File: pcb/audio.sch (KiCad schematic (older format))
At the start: 32 parts, among them J1 AudioJack3_SwitchTR, U400 CS43130, U401 ADP150-3.0, U402 ADP150-1.8, U403 ADP150-1.8, X1 DSC1001CE2-022.5792

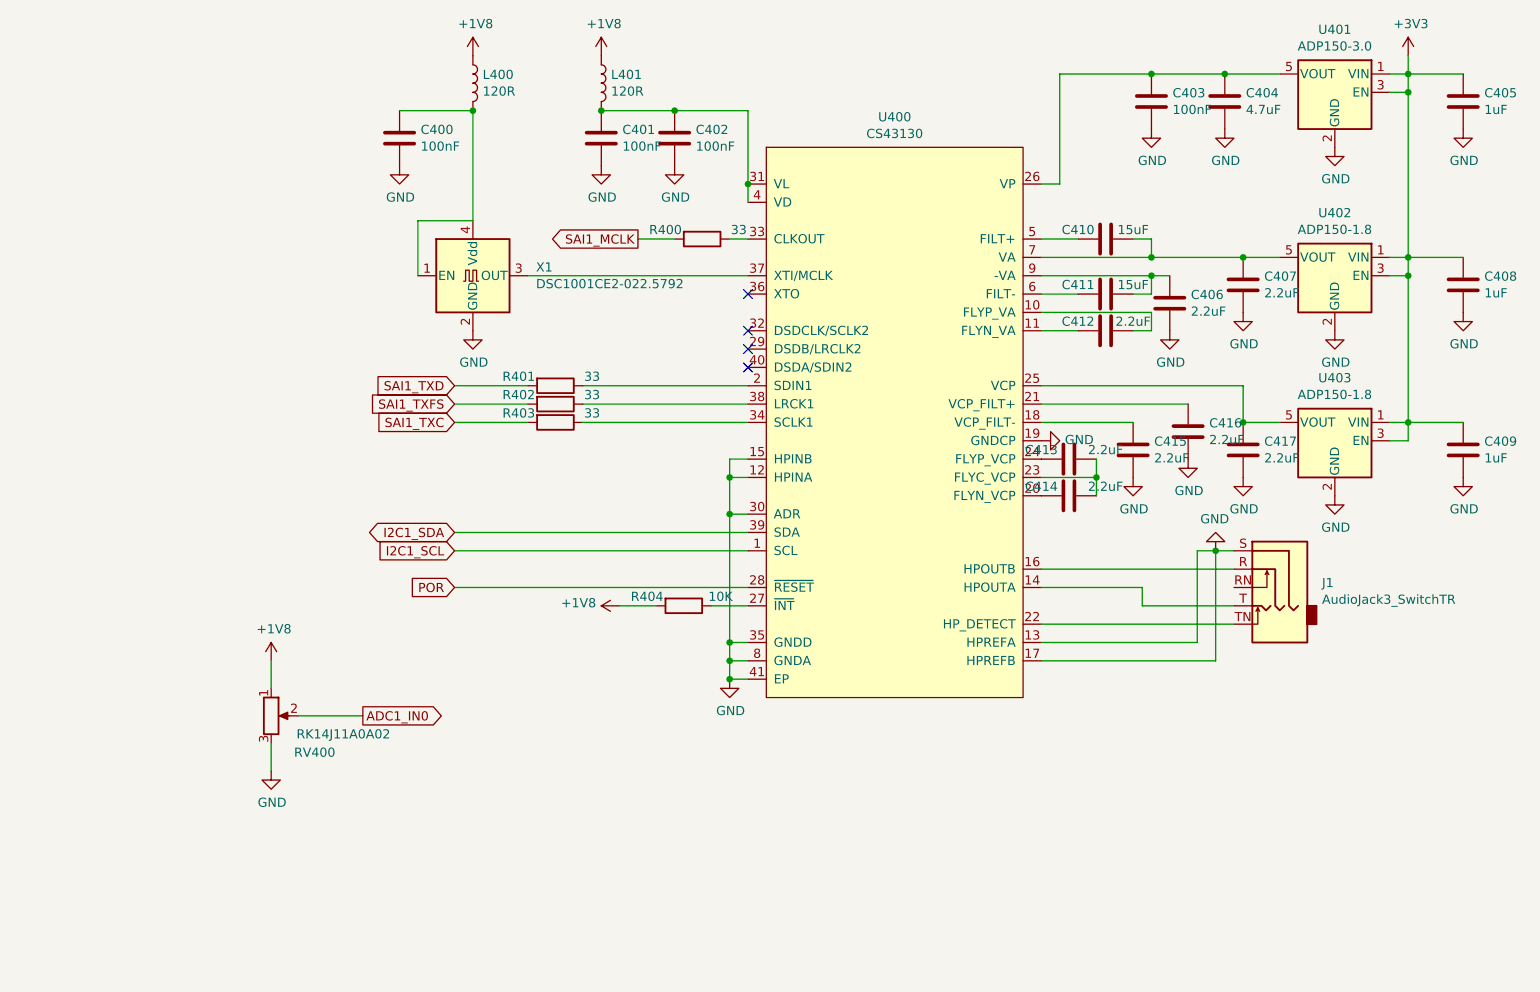
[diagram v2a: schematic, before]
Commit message: pcb: fixing voltage domain
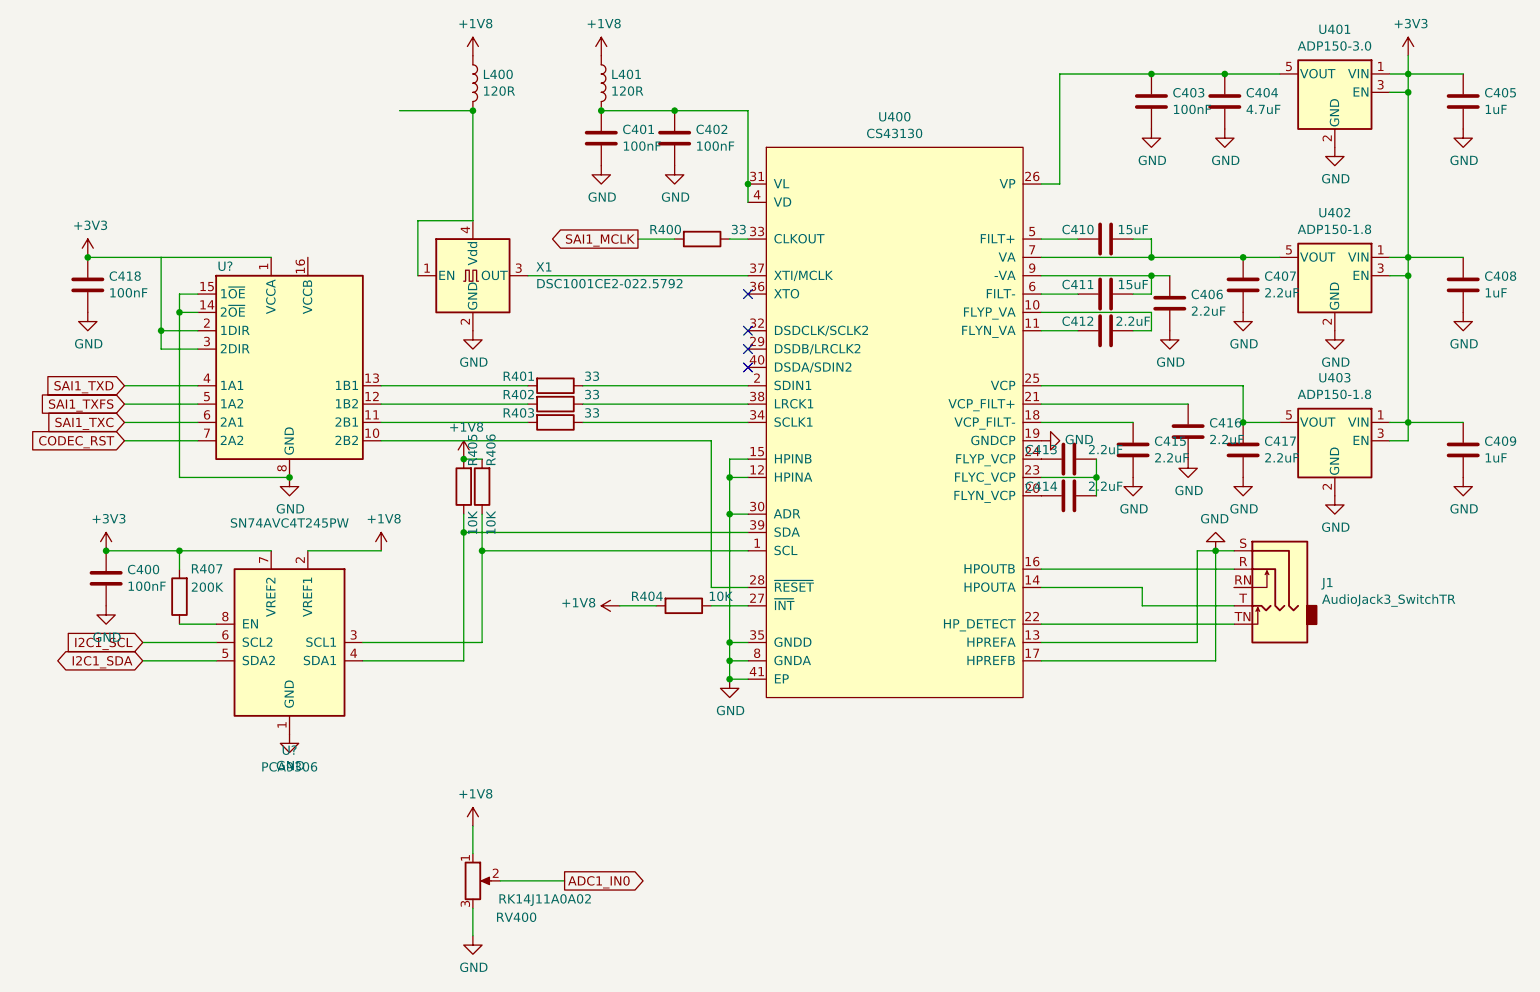
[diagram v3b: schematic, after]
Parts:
- added C418: 100nF, Capacitor_SMD:C_0402_1005Metric, symbol Device:C
- added R405, R406: 10K, Resistor_SMD:R_0603_1608Metric, symbol Device:R
- added R407: 200K, Resistor_SMD:R_0603_1608Metric, symbol Device:R
- added U?: SN74AVC4T245PW, Package_SO:TSSOP-16_4.4x5mm_P0.65mm, symbol Logic_LevelTranslator:SN74AVC4T245PW
- added U?: PCA9306, symbol Interface:PCA9306
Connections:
- net +1V8: now also R405.2, R406.2, U?.2 (VREF1)
- net +3V3: now also C400.1, C418.1, R407.2, U?.1 (VCCA), U?.2 (1DIR), U?.3 (2DIR), U?.7 (VREF2)
- net GND: now also C418.2, U?.1 (GND), U?.14 (2~OE), U?.15 (1~OE), U?.8 (GND), U?.9 (GND)
- net I2C1_SCL: now also U?.6 (SCL2); no longer U400.1 (SCL)
- net I2C1_SDA: now also U?.5 (SDA2); no longer U400.39 (SDA)
- net SAI1_TXC: now also U?.6 (2A1); no longer R403.2
- net SAI1_TXD: now also U?.4 (1A1); no longer R401.2
- net SAI1_TXFS: now also U?.5 (1A2); no longer R402.2
- net at L400.2, X1.1 (EN), X1.4 (Vdd): no longer C400.1
- net POR: no longer names the net of U400.28 (~RESET)
- net POR: now also U?.10 (2B2)
- new net: R406.1, U400.1 (SCL), U?.3 (SCL1)
- new net: R405.1, U400.39 (SDA), U?.4 (SDA1)
- new net: R401.2, U?.13 (1B1)
- new net: R402.2, U?.12 (1B2)
- new net: R403.2, U?.11 (2B1)
- new net: R407.1, U?.8 (EN)
- new net CODEC_RST: U?.7 (2A2)
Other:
- moved on the sheet: C400, RV400

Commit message: pcb: fixing i2c numbering; add filtering for lcd
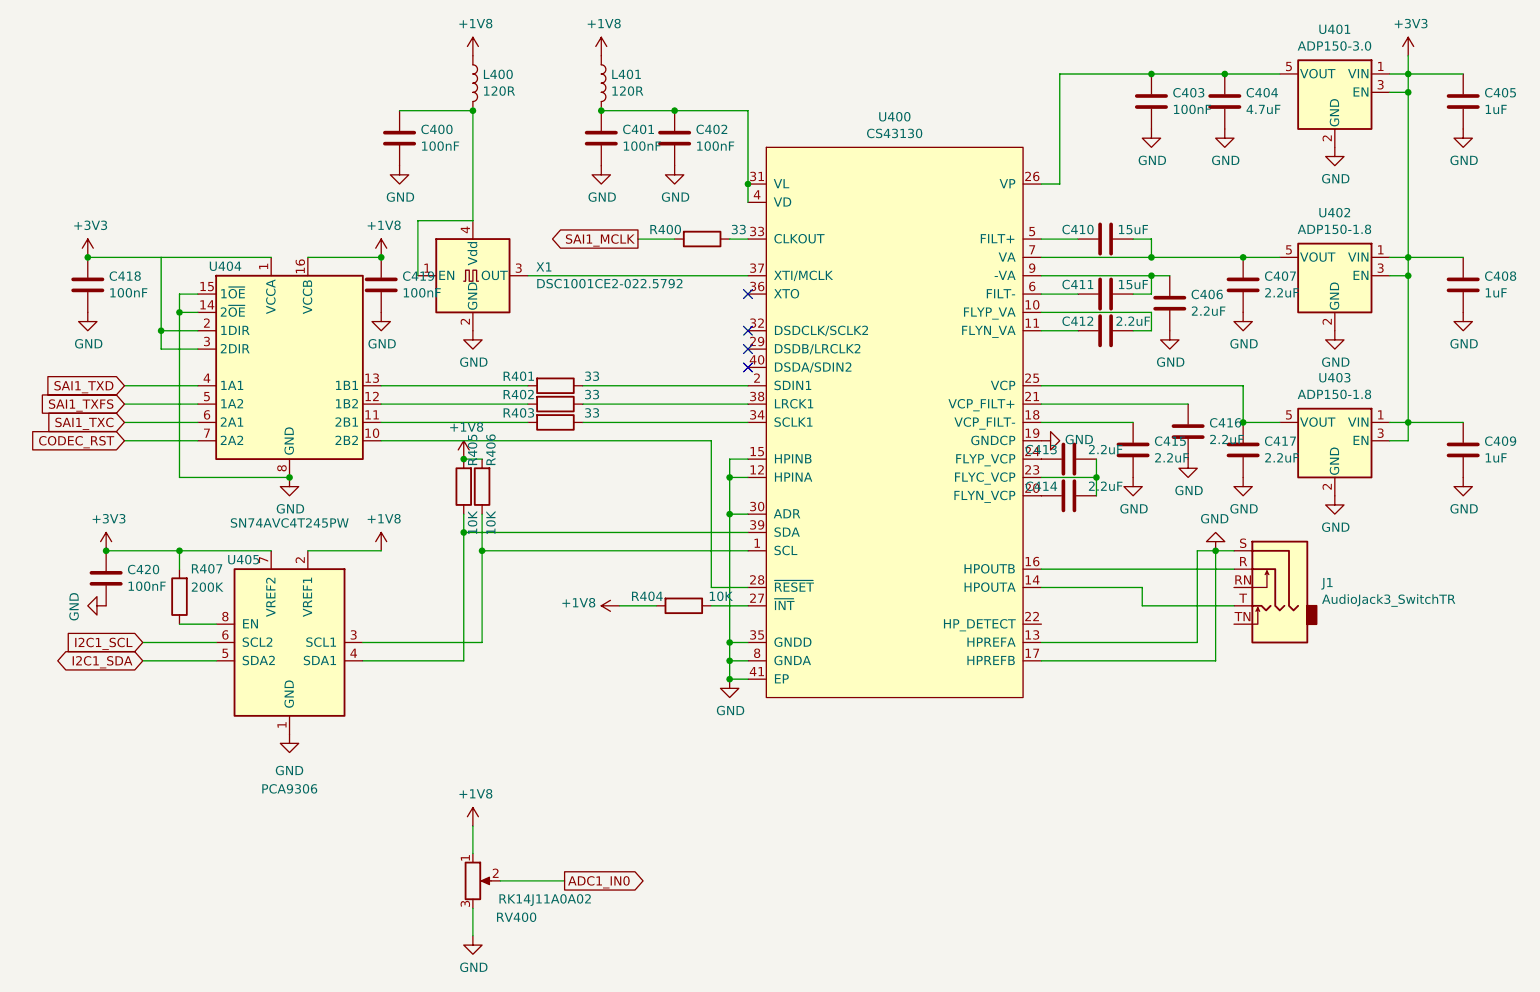
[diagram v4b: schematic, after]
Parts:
- added C419, C420: 100nF, Capacitor_SMD:C_0402_1005Metric, symbol Device:C
- U405: renamed from U?; footprint (none) -> Package_SO:VSSOP-8_2.3x2mm_P0.5mm
- gave numbers to parts that had none: 1
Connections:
- net +1V8: now also U404.16 (VCCB), C419.1
- net +3V3: now also C420.1; no longer C400.1
- net GND: now also C419.2, C420.2
- net at U400.22 (HP_DETECT): no longer J1.TN
- net at L400.2, X1.1 (EN), X1.4 (Vdd): now also C400.1
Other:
- moved on the sheet: C400
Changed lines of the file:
@@
 L Device:C C400
 U 1 1 5D487832
-P 1500 5150
-F 0 "C400" H 1615 5196 50  0000 L CNN
-F 1 "100nF" H 1615 5105 50  0000 L CNN
-F 2 "Capacitor_SMD:C_0402_1005Metric" H 1538 5000 50  0001 C CNN
-F 3 "~" H 1500 5150 50  0001 C CNN
-	1    1500 5150
+P 3100 2750
+F 0 "C400" H 3215 2796 50  0000 L CNN
+F 1 "100nF" H 3215 2705 50  0000 L CNN
+F 2 "Capacitor_SMD:C_0402_1005Metric" H 3138 2600 50  0001 C CNN
+F 3 "~" H 3100 2750 50  0001 C CNN
+	1    3100 2750
 	1    0    0    -1
 $EndComp
@@
 L power:GND #PWR0273
 U 1 1 5D487838
-P 1500 5300
-F 0 "#PWR0273" H 1500 5050 50  0001 C CNN
-F 1 "GND" H 1505 5127 50  0000 C CNN
-F 2 "" H 1500 5300 50  0001 C CNN
-F 3 "" H 1500 5300 50  0001 C CNN
-	1    1500 5300
+P 3100 2900
+F 0 "#PWR0273" H 3100 2650 50  0001 C CNN
+F 1 "GND" H 3105 2727 50  0000 C CNN
+F 2 "" H 3100 2900 50  0001 C CNN
+F 3 "" H 3100 2900 50  0001 C CNN
+	1    3100 2900
 	1    0    0    -1
 $EndComp
@@
 $EndComp
 Wire Wire Line
-	6600 5400 7650 5400
-Wire Wire Line
 	5000 4500 4900 4500
 Wire Wire Line
@@
 $EndComp
 $Comp
-L Logic_LevelTranslator:SN74AVC4T245PW U?
+L Logic_LevelTranslator:SN74AVC4T245PW U404
 U 1 1 5D8C4C20
 P 2500 4000
-F 0 "U?" H 2150 4550 50  0000 C CNN
+F 0 "U404" H 2150 4550 50  0000 C CNN
 F 1 "SN74AVC4T245PW" H 2500 3150 50  0000 C CNN
 F 2 "Package_SO:TSSOP-16_4.4x5mm_P0.65mm" H 2500 3900 50  0001 C CNN
@@
 	3450 4900 5000 4900
 $Comp
-L Interface:PCA9306 U?
+L Interface:PCA9306 U405
 U 1 1 5D90AA81
 P 2500 5500
-F 0 "U?" H 2500 4911 50  0000 C CNN
-F 1 "PCA9306" H 2500 4820 50  0000 C CNN
-F 2 "" H 2100 5850 50  0001 C CNN
+F 0 "U405" H 2750 5950 50  0000 C CNN
+F 1 "PCA9306" H 2500 4700 50  0000 C CNN
+F 2 "Package_SO:VSSOP-8_2.3x2mm_P0.5mm" H 2100 5850 50  0001 C CNN
 F 3 "http://www.ti.com/lit/ds/symlink/pca9306.pdf" H 2200 5950 50  0001 C CNN
 	1    2500 5500
@@
 Connection ~ 3550 5000
 $Comp
-L power:+1V8 #PWR?
+L power:+1V8 #PWR0120
 U 1 1 5D939A35
 P 3450 4500
-F 0 "#PWR?" H 3450 4350 50  0001 C CNN
+F 0 "#PWR0120" H 3450 4350 50  0001 C CNN
 F 1 "+1V8" H 3465 4673 50  0000 C CNN
 F 2 "" H 3450 4500 50  0001 C CNN
@@
 	1600 4400 2000 4400
 $Comp
-L power:GND #PWR?
+L power:GND #PWR0121
 U 1 1 5D94B448
 P 2500 4600
-F 0 "#PWR?" H 2500 4350 50  0001 C CNN
+F 0 "#PWR0121" H 2500 4350 50  0001 C CNN
 F 1 "GND" H 2505 4427 50  0000 C CNN
 F 2 "" H 2500 4600 50  0001 C CNN
@@
 $EndComp
 $Comp
-L power:GND #PWR?
+L power:GND #PWR0122
 U 1 1 5D94B88B
 P 2500 6000
-F 0 "#PWR?" H 2500 5750 50  0001 C CNN
-F 1 "GND" H 2505 5827 50  0000 C CNN
+F 0 "#PWR0122" H 2500 5750 50  0001 C CNN
+F 1 "GND" H 2500 5800 50  0000 C CNN
 F 2 "" H 2500 6000 50  0001 C CNN
 F 3 "" H 2500 6000 50  0001 C CNN
@@
 $EndComp
 $Comp
-L power:+3V3 #PWR?
+L power:+3V3 #PWR0123
 U 1 1 5D94CDEF
 P 1500 5000
-F 0 "#PWR?" H 1500 4850 50  0001 C CNN
+F 0 "#PWR0123" H 1500 4850 50  0001 C CNN
 F 1 "+3V3" H 1515 5173 50  0000 C CNN
 F 2 "" H 1500 5000 50  0001 C CNN
@@
 Wire Wire Line
 	1500 5000 1900 5000
-Connection ~ 1500 5000
 Connection ~ 1900 5000
 Wire Wire Line
@@
 	1900 5400 2100 5400
 $Comp
-L power:+1V8 #PWR?
+L power:+1V8 #PWR0125
 U 1 1 5D975B7E
 P 3000 5000
-F 0 "#PWR?" H 3000 4850 50  0001 C CNN
+F 0 "#PWR0125" H 3000 4850 50  0001 C CNN
 F 1 "+1V8" H 3015 5173 50  0000 C CNN
 F 2 "" H 3000 5000 50  0001 C CNN
@@
 $EndComp
 $Comp
-L power:GND #PWR?
+L power:GND #PWR0139
 U 1 1 5D994C93
 P 1400 3700
-F 0 "#PWR?" H 1400 3450 50  0001 C CNN
+F 0 "#PWR0139" H 1400 3450 50  0001 C CNN
 F 1 "GND" H 1405 3527 50  0000 C CNN
 F 2 "" H 1400 3700 50  0001 C CNN
@@
 $EndComp
 $Comp
-L power:+3V3 #PWR?
+L power:+3V3 #PWR0140
 U 1 1 5D994C99
 P 1400 3400
-F 0 "#PWR?" H 1400 3250 50  0001 C CNN
+F 0 "#PWR0140" H 1400 3250 50  0001 C CNN
 F 1 "+3V3" H 1415 3573 50  0000 C CNN
 F 2 "" H 1400 3400 50  0001 C CNN
@@
 	1400 3400 1800 3400
 Connection ~ 1400 3400
+$Comp
+L power:+1V8 #PWR?
+U 1 1 5DA41BB7
+P 3000 3400
+F 0 "#PWR?" H 3000 3250 50  0001 C CNN
+F 1 "+1V8" H 3015 3573 50  0000 C CNN
+F 2 "" H 3000 3400 50  0001 C CNN
+F 3 "" H 3000 3400 50  0001 C CNN
+	1    3000 3400
+	1    0    0    -1
+$EndComp
+Wire Wire Line
+	2600 3400 3000 3400
+$Comp
+L Device:C C419
+U 1 1 5DA47791
+P 3000 3550
+F 0 "C419" H 3115 3596 50  0000 L CNN
+F 1 "100nF" H 3115 3505 50  0000 L CNN
+F 2 "Capacitor_SMD:C_0402_1005Metric" H 3038 3400 50  0001 C CNN
+F 3 "~" H 3000 3550 50  0001 C CNN
+	1    3000 3550
+	1    0    0    -1
+$EndComp
+Connection ~ 3000 3400
+$Comp
+L power:GND #PWR?
+U 1 1 5DA4A9B1
+P 3000 3700
+F 0 "#PWR?" H 3000 3450 50  0001 C CNN
+F 1 "GND" H 3005 3527 50  0000 C CNN
+F 2 "" H 3000 3700 50  0001 C CNN
+F 3 "" H 3000 3700 50  0001 C CNN
+	1    3000 3700
+	1    0    0    -1
+$EndComp
+$Comp
+L Device:C C420
+U 1 1 5DA55A0F
+P 1500 5150
+F 0 "C420" H 1615 5196 50  0000 L CNN
+F 1 "100nF" H 1615 5105 50  0000 L CNN
+F 2 "Capacitor_SMD:C_0402_1005Metric" H 1538 5000 50  0001 C CNN
+F 3 "~" H 1500 5150 50  0001 C CNN
+	1    1500 5150
+	1    0    0    -1
+$EndComp
+Connection ~ 1500 5000
+$Comp
+L power:GND #PWR?
+U 1 1 5DA56209
+P 1500 5300
+F 0 "#PWR?" H 1500 5050 50  0001 C CNN
+F 1 "GND" H 1505 5127 50  0000 C CNN
+F 2 "" H 1500 5300 50  0001 C CNN
+F 3 "" H 1500 5300 50  0001 C CNN
+	1    1500 5300
+	0    1    1    0
+$EndComp
 $EndSCHEMATC
